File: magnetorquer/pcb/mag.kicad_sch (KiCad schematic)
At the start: 0 parts

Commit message: Alt det der manglede til Kicad
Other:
- added sheet ESP32 (ESP32.kicad_sch)
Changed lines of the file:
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@@
 	(paper "A4")
 	(sheet
-		(at 58.42 55.88)
+		(at 35.56 101.6)
 		(size 36.83 19.05)
 		(exclude_from_sim no)
@@
 		)
 		(property "Sheetname" "ACS_mag"
-			(at 58.42 55.1684 0)
+			(at 35.56 100.8884 0)
 			(effects
 				(font
@@
 		)
 		(property "Sheetfile" "acs_magnetorquer.kicad_sch"
-			(at 58.42 75.5146 0)
+			(at 35.56 121.2346 0)
 			(effects
 				(font
@@
 		)
 		(pin "mag1_neg" input
-			(at 58.42 69.85 180)
+			(at 35.56 115.57 180)
 			(effects
 				(font
@@
 		)
 		(pin "mag1_pos" input
-			(at 58.42 59.69 180)
+			(at 35.56 105.41 180)
 			(effects
 				(font
@@
 		)
 		(pin "mag2_neg" input
-			(at 95.25 69.85 0)
+			(at 72.39 115.57 0)
 			(effects
 				(font
@@
 		)
 		(pin "mag2_pos" input
-			(at 95.25 59.69 0)
+			(at 72.39 105.41 0)
 			(effects
 				(font
@@
 	)
 	(sheet
-		(at 118.11 58.42)
+		(at 88.9 78.74)
+		(size 24.13 45.72)
+		(exclude_from_sim no)
+		(in_bom yes)
+		(on_board yes)
+		(dnp no)
+		(fields_autoplaced yes)
+		(stroke
+			(width 0.1524)
+			(type solid)
+		)
+		(fill
+			(color 0 0 0 0.0000)
+		)
+		(property "Sheetname" "ESP32"
+			(at 88.9 78.0284 0)
+			(effects
+				(font
+					(size 1.27 1.27)
+				)
+				(justify left bottom)
+			)
+		)
+		(property "Sheetfile" "ESP32.kicad_sch"
+			(at 88.9 125.0446 0)
+			(effects
+				(font
+					(size 1.27 1.27)
+				)
+				(justify left top)
+			)
+		)
+		(instances
+			(project "mag"
+				(path "/14c04de7-71ee-4f20-9e6e-041dbb035733"
+					(page "4")
+				)
+			)
+		)
+	)
+	(sheet
+		(at 105.41 63.5)
 		(size 19.05 8.89)
 		(exclude_from_sim no)
@@
 		)
 		(property "Sheetname" "MPU-9255"
-			(at 118.11 57.7084 0)
+			(at 105.41 62.7884 0)
 			(effects
 				(font
@@
 		)
 		(property "Sheetfile" "mpu_9255.kicad_sch"
-			(at 118.11 67.8946 0)
+			(at 105.41 72.9746 0)
 			(effects
 				(font

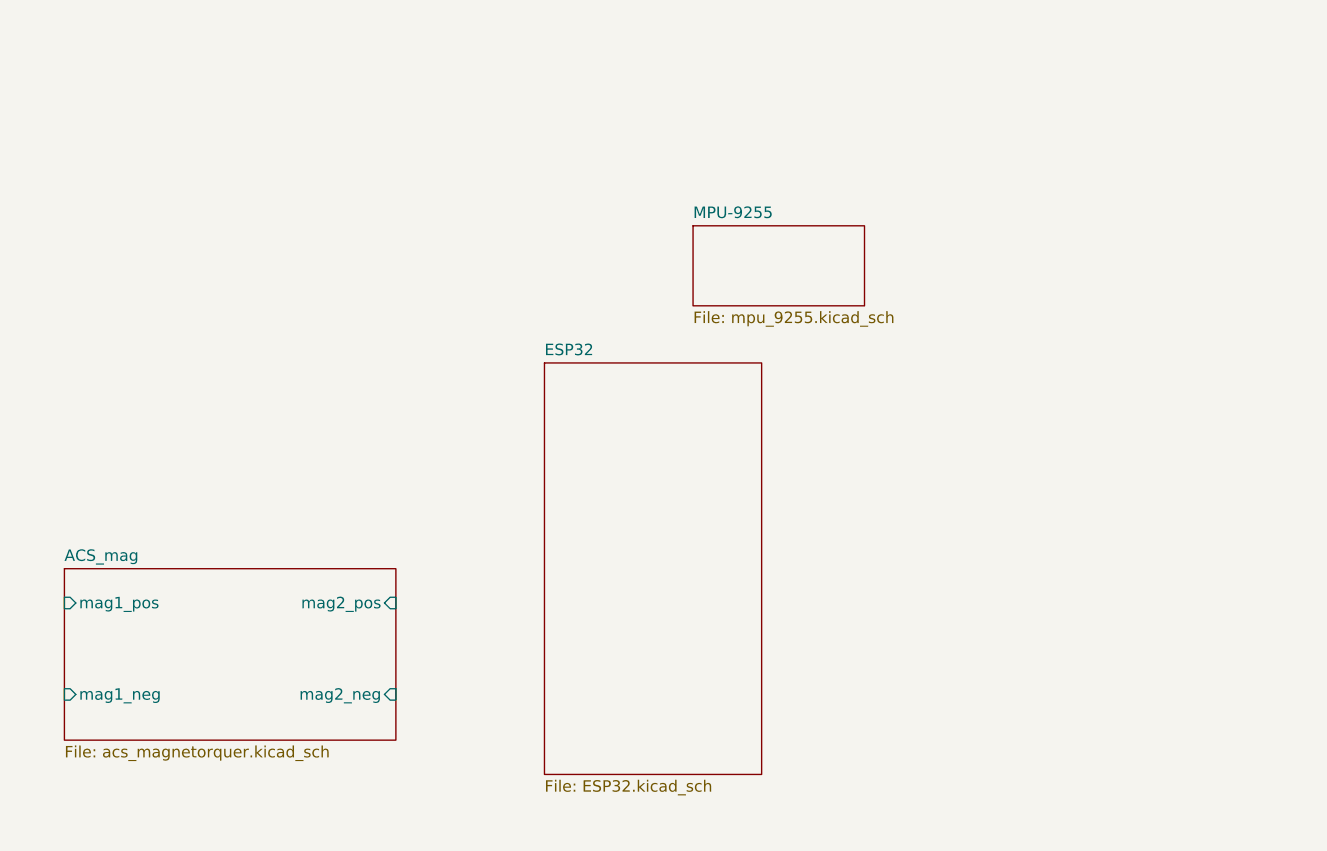
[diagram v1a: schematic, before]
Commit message: feat: lilygo s3 sch/footprint clean up sch
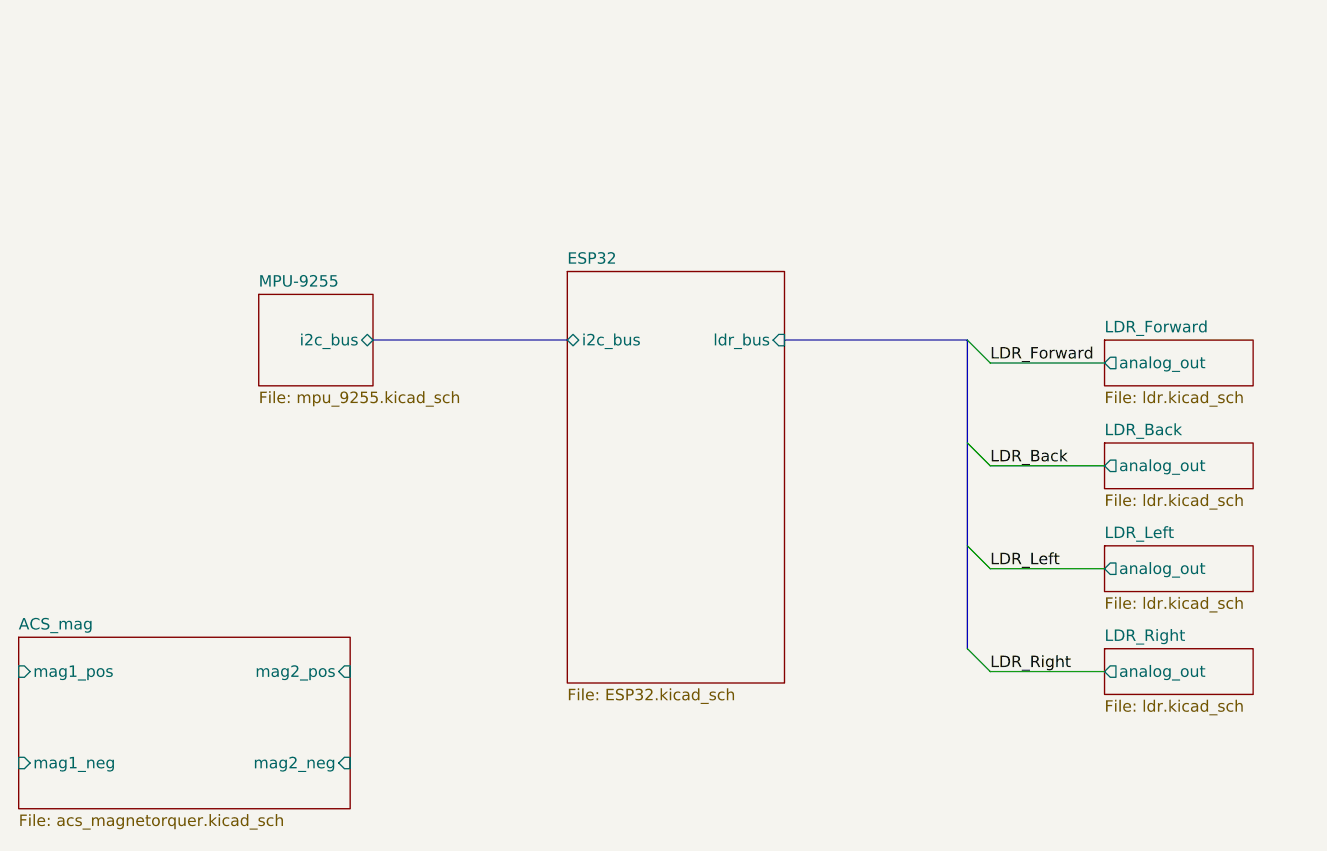
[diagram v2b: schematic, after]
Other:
- added sheet LDR_Back (ldr.kicad_sch)
- added sheet LDR_Forward (ldr.kicad_sch)
- added sheet LDR_Left (ldr.kicad_sch)
- added sheet LDR_Right (ldr.kicad_sch)
- sheet ESP32 ports: added i2c_bus, ldr_bus; removed none
- sheet MPU-9255 ports: added i2c_bus; removed none

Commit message: start routing pcb
It needs a power regulator and a battery terminal
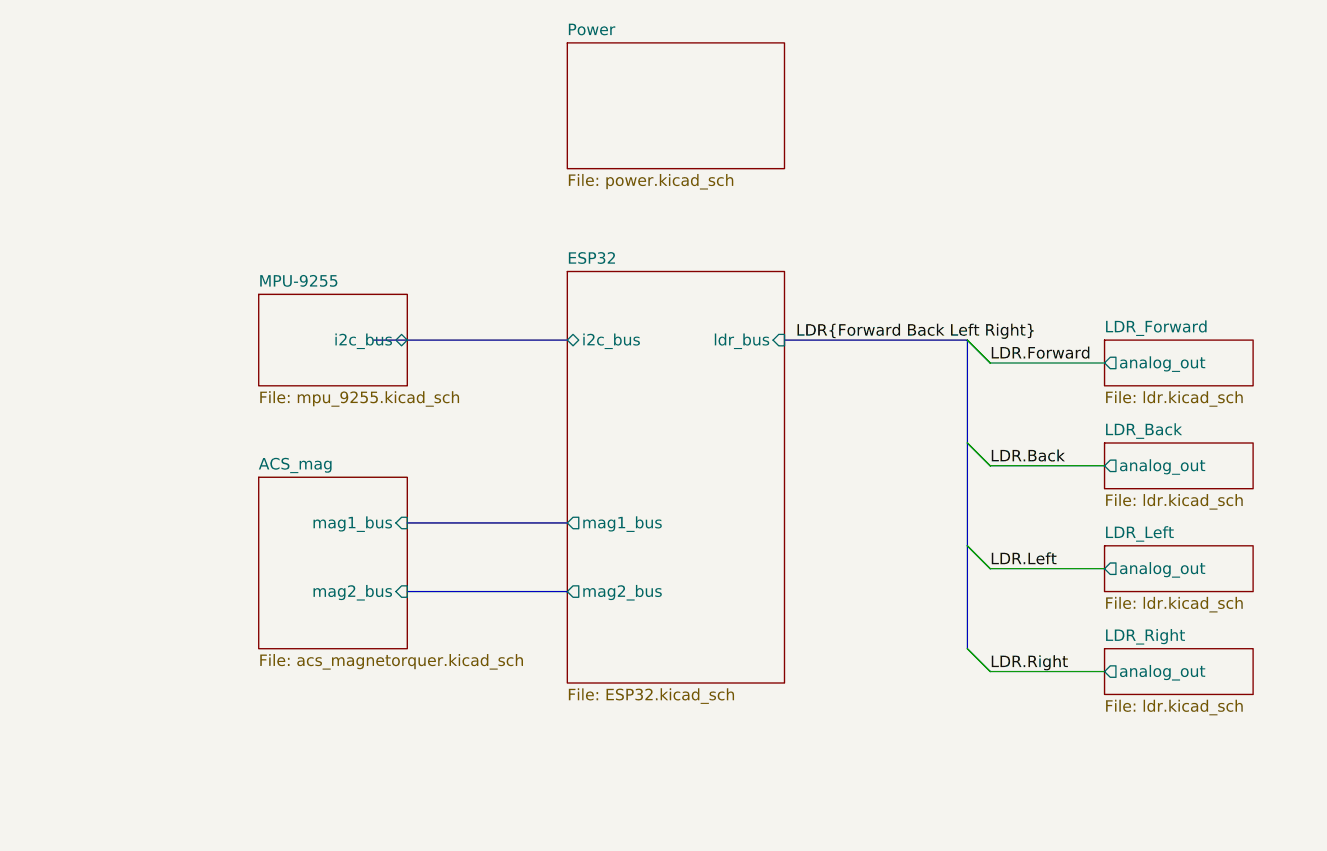
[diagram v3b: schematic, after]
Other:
- added sheet Power (power.kicad_sch)
- sheet ACS_mag ports: added mag1_bus, mag2_bus; removed mag1_neg, mag1_pos, mag2_neg, mag2_pos
- sheet ESP32 ports: added mag1_bus, mag2_bus; removed none
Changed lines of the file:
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@@
+	)
+	(bus_entry
+		(at 135.89 87.63)
+		(size 2.54 2.54)
+		(stroke
+			(width 0)
+			(type default)
+		)
+	)
+	(bus_entry
+		(at 135.89 110.49)
+		(size 2.54 2.54)
+		(stroke
+			(width 0)
+			(type default)
+		)
 	)
 	(bus_entry
@@
 		)
 	)
+	(bus_entry
+		(at 135.89 99.06)
+		(size 2.54 2.54)
+		(stroke
+			(width 0)
+			(type default)
+		)
+	)
+	(bus_entry
+		(at 135.89 76.2)
+		(size 2.54 2.54)
+		(stroke
+			(width 0)
+			(type default)
+		)
+	)
 	(bus
 		(pts
@@
 		)
 	)
+	(bus
+		(pts
+			(xy 73.66 96.52) (xy 91.44 96.52)
+		)
+		(stroke
+			(width 0)
+			(type default)
+		)
+	)
 	(wire
 		(pts
@@
 		)
 	)
+	(bus
+		(pts
+			(xy 73.66 104.14) (xy 91.44 104.14)
+		)
+		(stroke
+			(width 0)
+			(type default)
+		)
+	)
 	(wire
 		(pts
@@
 		)
 	)
-	(label "LDR_Left"
+	(label "LDR.Forward"
+		(at 138.43 78.74 0)
+		(effects
+			(font
+				(size 1.27 1.27)
+			)
+			(justify left bottom)
+		)
+	)
+	(label "LDR{Forward Back Left Right}"
+		(at 116.84 76.2 0)
+		(effects
+			(font
+				(size 1.27 1.27)
+			)
+			(justify left bottom)
+		)
+	)
+	(label "LDR.Back"
+		(at 138.43 90.17 0)
+		(effects
+			(font
+				(size 1.27 1.27)
+			)
+			(justify left bottom)
+		)
+	)
+	(label "LDR.Right"
+		(at 138.43 113.03 0)
+		(effects
+			(font
+				(size 1.27 1.27)
+			)
+			(justify left bottom)
+		)
+	)
+	(label "LDR.Left"
 		(at 138.43 101.6 0)
 		(effects
@@
 		)
 	)
-	(label "LDR_Back"
-		(at 138.43 90.17 0)
-		(effects
-			(font
-				(size 1.27 1.27)
-			)
-			(justify left bottom)
-		)
-	)
-	(label "LDR_Forward"
-		(at 138.43 78.74 0)
-		(effects
-			(font
-				(size 1.27 1.27)
-			)
-			(justify left bottom)
-		)
-	)
-	(label "LDR_Right"
-		(at 138.43 113.03 0)
-		(effects
-			(font
-				(size 1.27 1.27)
-			)
-			(justify left bottom)
-		)
-	)
-	(sheet
-		(at 30.48 109.22)
-		(size 36.83 19.05)
+	(sheet
+		(at 57.15 91.44)
+		(size 16.51 19.05)
 		(exclude_from_sim no)
 		(in_bom yes)
@@
 		)
 		(property "Sheetname" "ACS_mag"
-			(at 30.48 108.5084 0)
+			(at 57.15 90.7284 0)
 			(effects
 				(font
@@
 		)
 		(property "Sheetfile" "acs_magnetorquer.kicad_sch"
-			(at 30.48 128.8546 0)
-			(effects
-				(font
-					(size 1.27 1.27)
-				)
-				(justify left top)
-			)
-		)
-		(pin "mag1_neg" input
-			(at 30.48 123.19 180)
-			(effects
-				(font
-					(size 1.27 1.27)
-				)
-				(justify left)
-			)
-		)
-		(pin "mag1_pos" input
-			(at 30.48 113.03 180)
-			(effects
-				(font
-					(size 1.27 1.27)
-				)
-				(justify left)
-			)
-		)
-		(pin "mag2_neg" input
-			(at 67.31 123.19 0)
+			(at 57.15 111.0746 0)
+			(effects
+				(font
+					(size 1.27 1.27)
+				)
+				(justify left top)
+			)
+		)
+		(pin "mag1_bus" input
+			(at 73.66 96.52 0)
 			(effects
 				(font
@@
 			)
 		)
-		(pin "mag2_pos" input
-			(at 67.31 113.03 0)
+		(pin "mag2_bus" input
+			(at 73.66 104.14 0)
 			(effects
 				(font
@@
 			)
 		)
+		(pin "mag1_bus" output
+			(at 91.44 96.52 180)
+			(effects
+				(font
+					(size 1.27 1.27)
+				)
+				(justify left)
+			)
+		)
+		(pin "mag2_bus" output
+			(at 91.44 104.14 180)
+			(effects
+				(font
+					(size 1.27 1.27)
+				)
+				(justify left)
+			)
+		)
 		(instances
 			(project "mag"
@@
 	(sheet
 		(at 57.15 71.12)
-		(size 12.7 10.16)
+		(size 16.51 10.16)
 		(exclude_from_sim no)
 		(in_bom yes)
@@
 		)
 		(pin "i2c_bus" bidirectional
-			(at 69.85 76.2 0)
+			(at 73.66 76.2 0)
 			(effects
 				(font
@@
 				)
 			)
+		)
+	)
+	(sheet
+		(at 91.44 43.18)
+		(size 24.13 13.97)
+		(exclude_from_sim no)
+		(in_bom yes)
+		(on_board yes)
+		(dnp no)
+		(fields_autoplaced yes)
+		(stroke
+			(width 0.1524)
+			(type solid)
+		)
+		(fill
+			(color 0 0 0 0.0000)
+		)
+		(property "Sheetname" "Power"
+			(at 91.44 42.4684 0)
+			(effects
+				(font
+					(size 1.27 1.27)
+				)
+				(justify left bottom)
+			)
+		)
+		(property "Sheetfile" "power.kicad_sch"
+			(at 91.44 57.7346 0)
+			(effects
+				(font
+					(size 1.27 1.27)
+				)
+				(justify left top)
+			)
+		)
+		(instances
+			(project "mag"
+				(path "/14c04de7-71ee-4f20-9e6e-041dbb035733"
+					(page "9")
+				)
+			)
